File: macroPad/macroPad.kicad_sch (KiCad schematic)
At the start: 14 parts, among them SW1 SW_Push, U1 ATmega32U4-A, Y1 16MHz

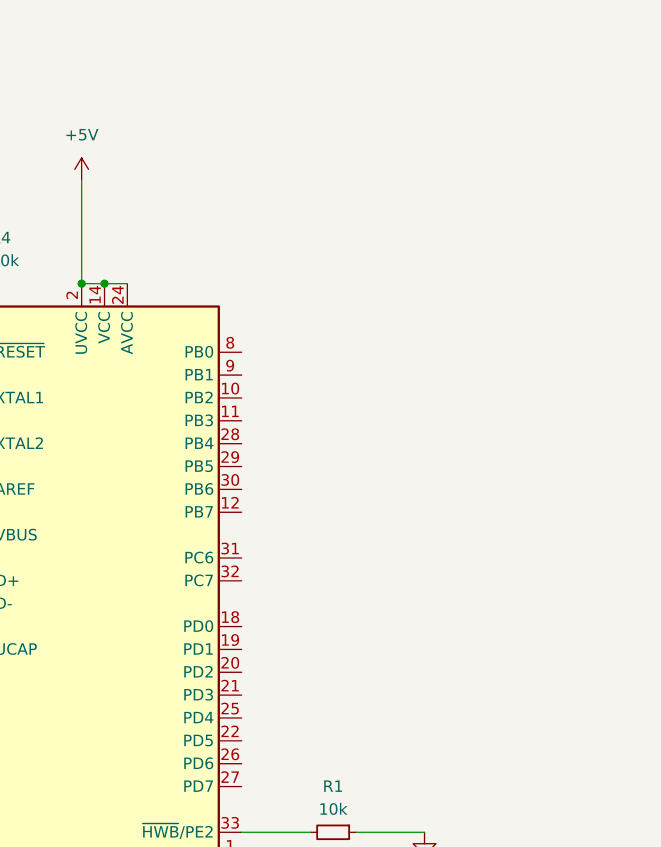
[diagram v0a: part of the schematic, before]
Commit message: switch matrix added
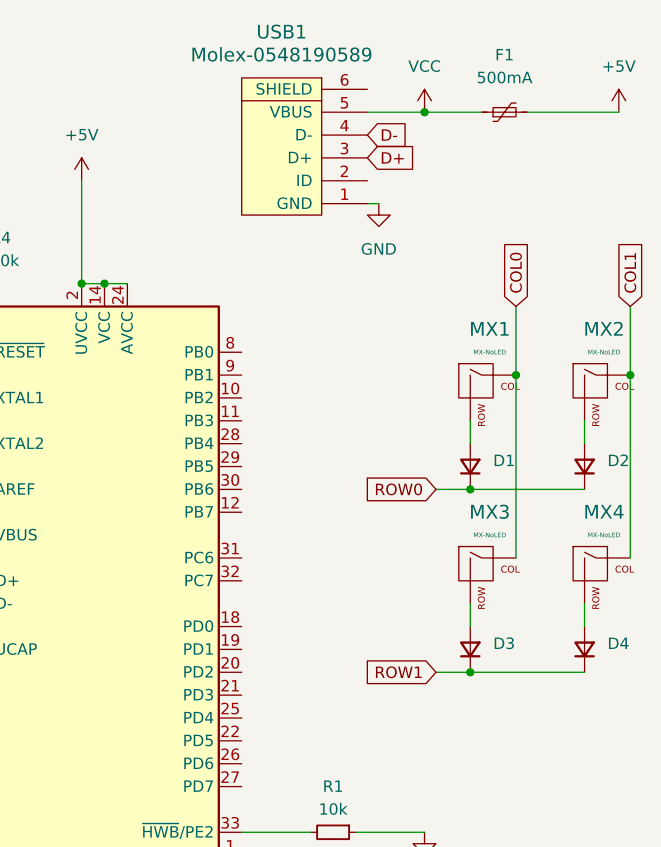
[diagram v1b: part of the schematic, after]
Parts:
- added D1, D2, D3, D4: ~, symbol Device:D_Small
- added F1: 500mA, symbol Device:Polyfuse_Small
- added MX1, MX2, MX3, MX4: MX-NoLED, symbol MX_Alps_Hybrid:MX-NoLED
- added USB1: Molex-0548190589, symbol random-keyboard-parts:Molex-0548190589
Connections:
- net +5V: now also F1.2
- net D+: now also USB1.3 (D+)
- net D-: now also USB1.4 (D-)
- net GND: now also USB1.1 (GND)
- new net: D3.2 (A), MX3.2 (ROW)
- new net: D4.2 (A), MX4.2 (ROW)
- new net: D2.2 (A), MX2.2 (ROW)
- new net: D1.2 (A), MX1.2 (ROW)
- new net COL0: MX1.1 (COL), MX3.1 (COL)
- new net COL1: MX2.1 (COL), MX4.1 (COL)
- new net ROW0: D1.1 (K), D2.1 (K)
- new net ROW1: D3.1 (K), D4.1 (K)
- new net VCC: F1.1, USB1.5 (VBUS)

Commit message: footprints
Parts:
- C1, C2, C3, C4, C5, C6, C7: footprint (none) -> Capacitor_SMD:C_0805_2012Metric
- D1, D2, D3, D4: footprint (none) -> Diode_SMD:D_SOD-123
- F1: footprint (none) -> Fuse:Fuse_1206_3216Metric
- MX1, MX2, MX3, MX4: footprint (none) -> MX_Alps_Hybrid:MX-1.5U-NoLED
- R1, R2, R3, R4: footprint (none) -> Resistor_SMD:R_0805_2012Metric
- SW1: footprint (none) -> random-keyboard-parts:SKQG-1155865
- USB1: footprint (none) -> random-keyboard-parts:Molex-0548190589
- Y1: footprint (none) -> Crystal:Crystal_SMD_3225-4Pin_3.2x2.5mm
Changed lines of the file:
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@@
 			)
 		)
-		(property "Footprint" ""
+		(property "Footprint" "Diode_SMD:D_SOD-123"
 			(at 179.07 95.25 90)
 			(effects
@@
 			)
 		)
-		(property "Footprint" ""
+		(property "Footprint" "MX_Alps_Hybrid:MX-1.5U-NoLED"
 			(at 177.165 86.995 0)
 			(effects
@@
 			)
 		)
-		(property "Footprint" ""
+		(property "Footprint" "random-keyboard-parts:Molex-0548190589"
 			(at 160.02 40.64 0)
 			(effects
@@
 			)
 		)
-		(property "Footprint" ""
+		(property "Footprint" "Capacitor_SMD:C_0805_2012Metric"
 			(at 99.06 120.65 0)
 			(effects
@@
 			)
 		)
-		(property "Footprint" ""
+		(property "Footprint" "Diode_SMD:D_SOD-123"
 			(at 191.77 74.93 90)
 			(effects
@@
 			)
 		)
-		(property "Footprint" ""
+		(property "Footprint" "MX_Alps_Hybrid:MX-1.5U-NoLED"
 			(at 177.165 66.675 0)
 			(effects
@@
 			)
 		)
-		(property "Footprint" ""
+		(property "Footprint" "Diode_SMD:D_SOD-123"
 			(at 179.07 74.93 90)
 			(effects
@@
 			)
 		)
-		(property "Footprint" ""
+		(property "Footprint" "Crystal:Crystal_SMD_3225-4Pin_3.2x2.5mm"
 			(at 110.49 69.85 0)
 			(effects
@@
 			)
 		)
-		(property "Footprint" ""
+		(property "Footprint" "Capacitor_SMD:C_0805_2012Metric"
 			(at 87.63 120.65 0)
 			(effects
@@
 			)
 		)
-		(property "Footprint" ""
+		(property "Footprint" "MX_Alps_Hybrid:MX-1.5U-NoLED"
 			(at 164.465 66.675 0)
 			(effects
@@
 			)
 		)
-		(property "Footprint" ""
+		(property "Footprint" "Resistor_SMD:R_0805_2012Metric"
 			(at 123.19 50.8 0)
 			(effects
@@
 			)
 		)
-		(property "Footprint" ""
+		(property "Footprint" "Capacitor_SMD:C_0805_2012Metric"
 			(at 109.22 120.65 0)
 			(effects
@@
 			)
 		)
-		(property "Footprint" ""
+		(property "Footprint" "MX_Alps_Hybrid:MX-1.5U-NoLED"
 			(at 164.465 86.995 0)
 			(effects
@@
 			)
 		)
-		(property "Footprint" ""
+		(property "Footprint" "Resistor_SMD:R_0805_2012Metric"
 			(at 163.83 115.57 0)
 			(effects
@@
 			)
 		)
-		(property "Footprint" ""
+		(property "Footprint" "Capacitor_SMD:C_0805_2012Metric"
 			(at 118.11 100.33 0)
 			(effects
@@
 			)
 		)
-		(property "Footprint" ""
+		(property "Footprint" "Capacitor_SMD:C_0805_2012Metric"
 			(at 77.47 120.65 0)
 			(effects
@@
 			)
 		)
-		(property "Footprint" ""
+		(property "Footprint" "Resistor_SMD:R_0805_2012Metric"
 			(at 114.3 87.63 0)
 			(effects
@@
 			)
 		)
-		(property "Footprint" ""
+		(property "Footprint" "Diode_SMD:D_SOD-123"
 			(at 191.77 95.25 90)
 			(effects
@@
 			)
 		)
-		(property "Footprint" ""
+		(property "Footprint" "random-keyboard-parts:SKQG-1155865"
 			(at 118.11 50.8 0)
 			(effects
@@
 			)
 		)
-		(property "Footprint" ""
+		(property "Footprint" "Resistor_SMD:R_0805_2012Metric"
 			(at 105.41 90.17 0)
 			(effects
@@
 			)
 		)
-		(property "Footprint" ""
+		(property "Footprint" "Fuse:Fuse_1206_3216Metric"
 			(at 187.96 34.29 0)
 			(effects
@@
 			)
 		)
-		(property "Footprint" ""
+		(property "Footprint" "Capacitor_SMD:C_0805_2012Metric"
 			(at 104.14 74.93 0)
 			(effects
@@
 			)
 		)
-		(property "Footprint" ""
+		(property "Footprint" "Capacitor_SMD:C_0805_2012Metric"
 			(at 97.79 66.04 0)
 			(effects
